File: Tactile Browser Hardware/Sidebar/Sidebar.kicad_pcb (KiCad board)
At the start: 2 copper layers, 38 parts, among them J1 Conn_01x02_Pin, J2 Conn_01x02_Pin, J3 Barrel_Jack_Switch, J4 Conn_01x02_Pin, SW10 SW_Push, SW11 SW_Push, SW12 SW_Push, SW6 SW_Push, SW7 SW_Push, SW8 SW_Push, SW9 SW_Push

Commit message: finished pcb placement
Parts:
- removed Kill_Switch_DC1: SW_SPST, Button_Switch_Keyboard:SW_Cherry_MX_1.00u_PCB
- 1000uf25V1, 1000uf25V2, 1000uf25V3, A1, D1, D10, D11, D12, D2, D3, D4, D6, D7, D8, D9, Fuse1, J1, J3, J4: moved to B.Cu
- J2: footprint TerminalBlock_MetzConnect:TerminalBlock_MetzConnect_Type094_RT03506HBLU_1x06_P5.00mm_Horizontal -> TerminalBlock_Phoenix:ScrewTerminal_Vertical_1935310; moved to B.Cu
- moved D8 115.3 mm to (182.8, 56.2), turned to 90 degrees
- moved D7 115.3 mm to (186.2, 56.2), turned to 90 degrees
- moved AudioSpeed1 110.3 mm to (212.8, 59.0)
- moved D11 109.6 mm to (189.0, 61.2), turned to -90 degrees
- moved 4.7k_ohm2 109.2 mm to (60.5, 65.5), turned to 90 degrees
- moved Volume1 108.4 mm to (194.2, 59.0)
- moved D12 108.1 mm to (189.0, 66.8), turned to 90 degrees
- moved 4.7k_ohm1 107.2 mm to (62.0, 65.5), turned to 90 degrees
- moved power_button1 106.2 mm to (49.5, 61.2)
- moved Fuse1 86.9 mm to (82.5, 72.8), turned to 180 degrees
- moved J4 86.1 mm to (116.9, 66.2), turned to 180 degrees
- moved D3 85.6 mm to (121.0, 55.2), turned to -90 degrees
- moved D5 85.0 mm to (56.8, 61.2), turned to 90 degrees
- moved D6 84.8 mm to (138.2, 56.6), turned to 90 degrees
- moved J1 83.4 mm to (106.8, 66.2), turned to 180 degrees
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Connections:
- Fuse1 pad 2: Net-(Kill_Switch_DC1-A) -> 12V
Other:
- board outline added: 200.8 x 22.8 mm

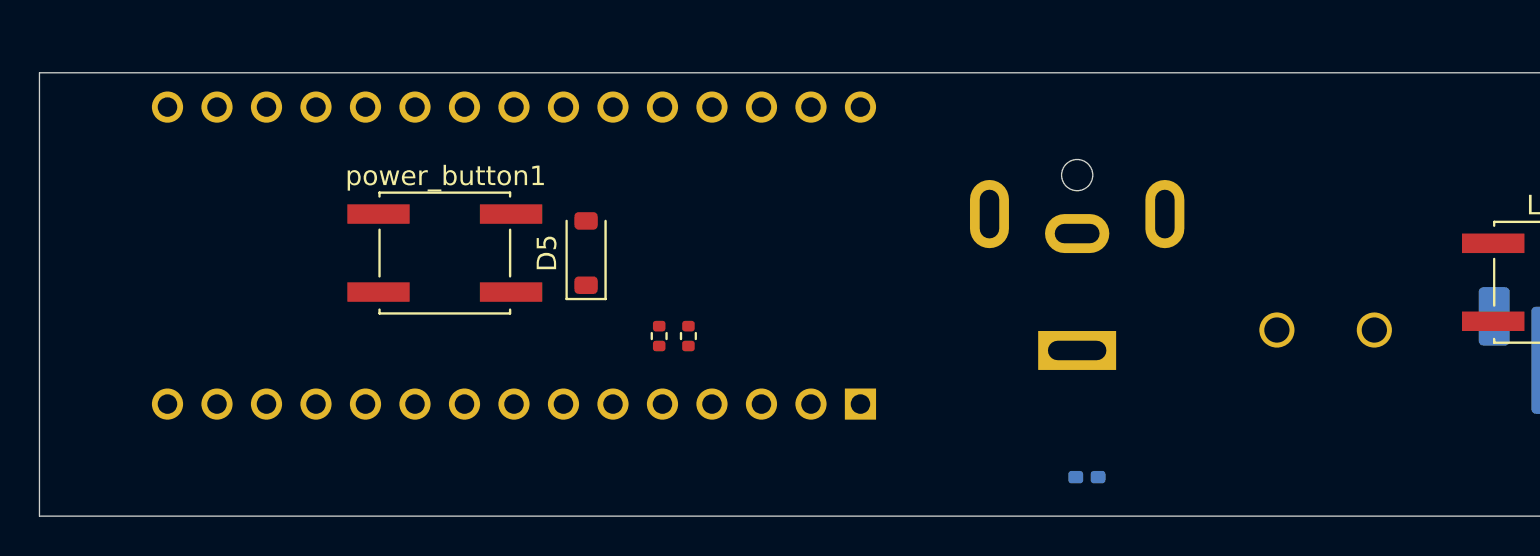
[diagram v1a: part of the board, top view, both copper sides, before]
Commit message: finally got the right fuse
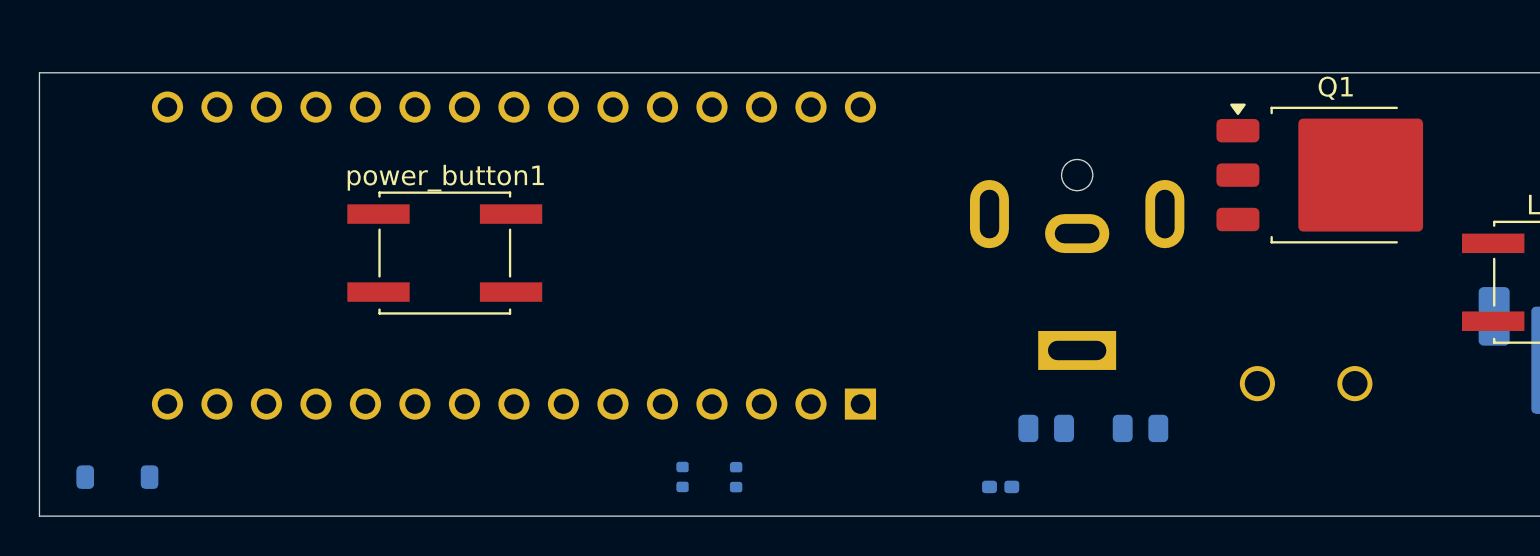
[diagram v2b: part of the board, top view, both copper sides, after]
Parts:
- added 100kR1: R, Resistor_SMD:R_0805_2012Metric, B.Cu at (85.2, 70.2)
- added 1kR1: R, Resistor_SMD:R_0805_2012Metric, B.Cu at (80.4, 70.2)
- added Q1: PMOS, Package_TO_SOT_SMD:TO-252-3_TabPin2, F.Cu at (95.3, 57.2)
- 4.7k_ohm1, 4.7k_ohm2, D5: moved to B.Cu
- moved D5 26.7 mm to (32.8, 72.8), turned to 0 degrees
- moved 4.7k_ohm1 7.64 mm to (64.5, 72.8)
- moved 4.7k_ohm2 7.33 mm to (61.8, 72.7)
- moved Fuse1 4.46 mm to (78.1, 73.2)
- moved J2 2.93 mm to (91.2, 68.0)
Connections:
- 1000uf25V1 pad 1: 12V -> Net-(J2-Pin_2)
- 1000uf25V2 pad 1: 12V -> Net-(J2-Pin_2)
- 1000uf25V3 pad 1: 12V -> Net-(J2-Pin_2)
- A1 pad 26: unconnected-(A1-A7-Pad26) -> A7
- Fuse1 pad 2: 12V -> Net-(Q1-S)
- J1 pad 1: SCL -> SDA
- J1 pad 2: SDA -> SCL
- J2 pad 1: 12V -> GND
- J2 pad 2: GND -> Net-(J2-Pin_2)
- J4 pad 2: GND -> 5V

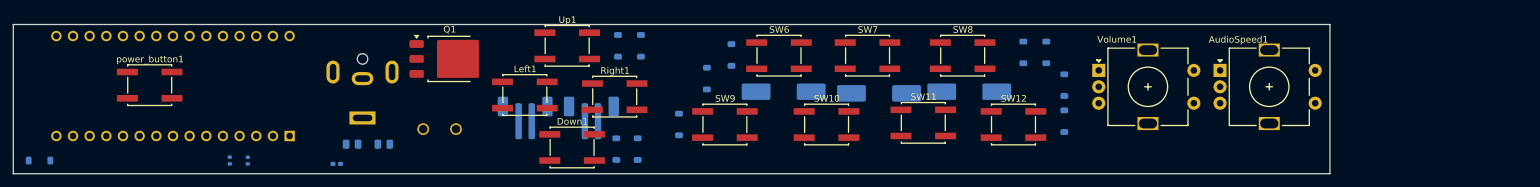
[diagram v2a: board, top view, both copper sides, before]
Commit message: footprint placement
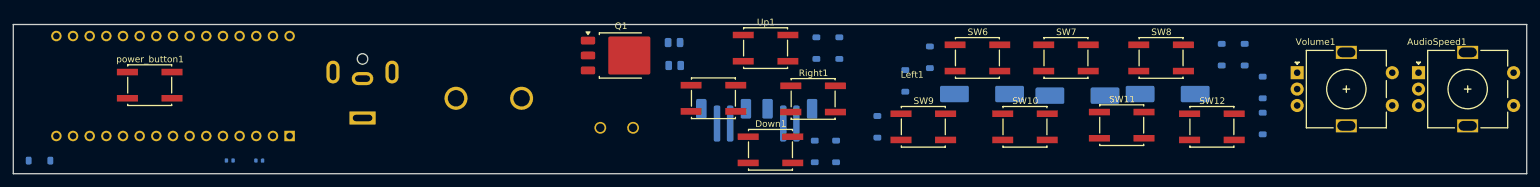
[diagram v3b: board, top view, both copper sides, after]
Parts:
- Fuse1: footprint Fuse:Fuse_0402_1005Metric_Pad0.77x0.64mm_HandSolder -> fuse_3560:FUSE_3560
- moved 1kR1 51.5 mm to (129.5, 54.8)
- moved 100kR1 45.9 mm to (129.6, 58.2)
- moved J1 30.3 mm to (137.1, 66.6)
- moved 1000uf25V1 30.3 mm to (176.4, 62.6)
- moved 1000uf25V2 30.3 mm to (204.8, 62.6)
- moved 1000uf25V3 30.3 mm to (191.0, 62.9)
- moved AudioSpeed1 30.3 mm to (243.0, 59.4)
- moved D10 30.3 mm to (164.8, 60.6)
- moved D11 30.3 mm to (219.2, 61.6)
- moved D12 30.3 mm to (219.2, 67.1)
- moved D6 30.3 mm to (168.5, 57.0)
- moved D7 30.3 mm to (216.5, 56.6)
- moved D8 30.3 mm to (213.0, 56.6)
- moved D9 30.3 mm to (160.5, 67.6)
- moved J4 30.3 mm to (147.2, 66.6)
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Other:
- board size 200.8 x 22.8 mm -> 230.8 x 22.8 mm

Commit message: sidebar pcb progress
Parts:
- Q1: moved to B.Cu
- moved 4.7k_ohm2 14.8 mm to (76.5, 72.8), turned to -90 degrees
- moved 4.7k_ohm1 14.0 mm to (80.2, 72.8), turned to 90 degrees
- moved D4 8.61 mm to (158.2, 63.8), turned to 90 degrees
- moved D9 7.36 mm to (163.8, 61.0), turned to -90 degrees
- moved D2 7.35 mm to (158.2, 70.5)
- moved 100kR1 5.76 mm to (134.5, 55.2), turned to -90 degrees
- moved D10 5.20 mm to (163.8, 55.5)
- moved power_button1 3.09 mm to (47.0, 63.0)
- moved D1 3.05 mm to (157.8, 55.5)
- moved D6 1.46 mm to (167.8, 55.8)
- moved D11 1.37 mm to (219.5, 60.2)
- moved D3 1.30 mm to (152.5, 55.6)
- moved Down1 0.96 mm to (143.2, 71.0)
- moved 1kR1 0.56 mm to (129.8, 55.2), turned to -90 degrees
- moved J2 0.32 mm to (118.0, 68.0)
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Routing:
- net AS1: track 0.00 -> 211.1 mm, vias 0 -> 1
- net AS2: track 0.00 -> 204.3 mm, vias 0 -> 1
- net Col2: track 0.00 -> 183.3 mm, vias 0 -> 5
- net RE1: track 0.00 -> 180.2 mm
- net RE2: track 0.00 -> 179.4 mm
- net Col3: track 0.00 -> 176.6 mm, vias 0 -> 2
- net Col1: track 0.00 -> 165.6 mm
- net 5V: track 0.00 -> 104.4 mm, vias 0 -> 1
- net SDA: track 0.00 -> 100.2 mm
- net SCL: track 0.00 -> 96.9 mm, vias 0 -> 3
- net Row3: track 0.00 -> 76.8 mm
- net Net-(D7-A): track 0.00 -> 33.0 mm, vias 0 -> 1
- net Row1: track 0.00 -> 30.8 mm
- net Net-(D10-A): track 0.00 -> 26.7 mm, vias 0 -> 1
- net Net-(D11-A): track 0.00 -> 26.7 mm, vias 0 -> 1
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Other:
- board size 230.8 x 22.8 mm -> 230.8 x 24 mm
- board text added: "5V"
- board text added: "GND"
- board text added: "JAck"
- board text added: "SCL"

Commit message: done with pcb connections
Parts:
- moved power_button1 2.15 mm to (45.8, 61.2)
- moved J3 1.25 mm to (82.0, 65.0)
- moved D5 0.50 mm to (32.8, 73.2)
- moved 1kR1 0.35 mm to (129.5, 55.5), turned to 90 degrees
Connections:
- 1kR1 pad 2: A7 -> D12_mosfet
- A1 pad 26: A7 -> unconnected-(A1-A7-Pad26)
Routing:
- net Row4: track 18.5 -> 156.8 mm, vias 0 -> 4
- net Row3: track 76.8 -> 207.2 mm, vias 0 -> 2
- net GND: track 18.5 -> 145.3 mm, vias 0 -> 10
- net Row2: track 22.8 -> 144.8 mm, vias 0 -> 2
- net Row1: track 30.8 -> 151.2 mm, vias 0 -> 2
- net D12_mosfet: track 0.00 -> 103.5 mm, vias 0 -> 1
- net Net-(100kR1-Pad2): track 0.00 -> 61.5 mm
- net Net-(D5-A): track 0.00 -> 27.8 mm, vias 0 -> 1
- net Net-(Q1-S): track 0.00 -> 23.8 mm
- net Net-(Q1-G): track 0.00 -> 19.1 mm
- net Net-(J2-Pin_2): track 0.00 -> 17.1 mm, vias 0 -> 1
- net Col2: track 183.3 -> 182.7 mm
- net SDA: track 100.2 -> 100.5 mm, vias 0 -> 2

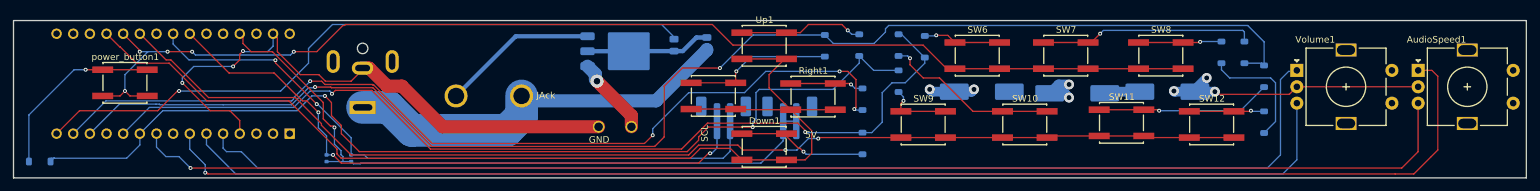
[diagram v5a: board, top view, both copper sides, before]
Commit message: finished filled zones! (sidebar)
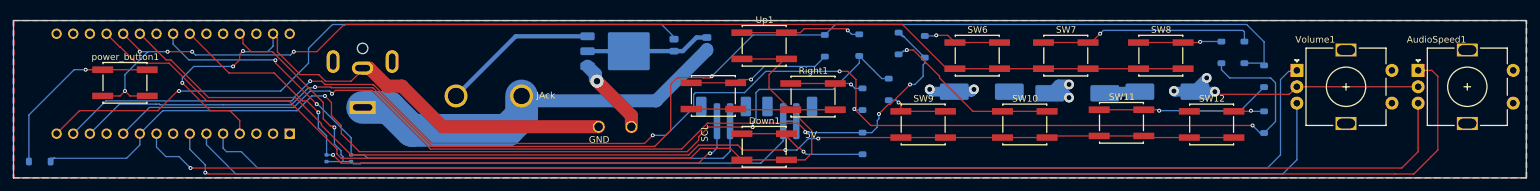
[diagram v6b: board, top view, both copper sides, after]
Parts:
- moved D9 1.95 mm to (162.2, 62.2)
- moved D10 0.25 mm to (163.8, 55.2)
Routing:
- net Row4: track 156.8 -> 221.4 mm, vias 4 -> 5
- net Row3: track 207.2 -> 205.6 mm
- net Row1: track 151.2 -> 150.2 mm
- net Net-(D3-A): track 23.0 -> 22.1 mm
- net Net-(D1-A): track 18.8 -> 18.3 mm
- net Row2: track 144.8 -> 145.3 mm, vias 2 -> 4
- added copper zone on F.Cu, net GND
- added copper zone on B.Cu, net Net-(J2-Pin_2)

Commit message: FINISHED SIDEBAR
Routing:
- net GND: track 145.3 -> 147.4 mm
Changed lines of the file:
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@@
+	)
+	(segment
+		(start 243 61.85)
+		(end 244.85 61.85)
+		(width 0.2)
+		(layer "F.Cu")
+		(net 4)
 	)
 	(segment
@@
 		(width 0.2)
 		(layer "F.Cu")
+		(net 4)
+	)
+	(segment
+		(start 244.85 61.85)
+		(end 245 62)
+		(width 0.2)
+		(layer "F.Cu")

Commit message: added m2 screws
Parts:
- added REF**: MountingHole_2.2mm_M2, MountingHole:MountingHole_2.2mm_M2, F.Cu at (262.8, 71.5)
- added REF**: MountingHole_2.2mm_M2, MountingHole:MountingHole_2.2mm_M2, F.Cu at (262.8, 56.0)
- added REF**: MountingHole_2.2mm_M2, MountingHole:MountingHole_2.2mm_M2, F.Cu at (33.2, 73.8)
- moved D5 12.0 mm to (44.8, 73.8)
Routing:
- net Row1: track 150.2 -> 139.3 mm
- net Net-(D5-A): track 27.8 -> 36.6 mm
- net Row2: track 145.3 -> 146.2 mm
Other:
- board size 230.8 x 24 mm -> 237.5 x 25 mm
